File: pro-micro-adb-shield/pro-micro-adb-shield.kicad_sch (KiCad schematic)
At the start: 9 parts, among them J1 Mini-DIN-4, SW1 SW_Push_Dual, SW2 SW_DIP_x04, U1 Arduino_Pro_Micro

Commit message: Fix shorted RST/GND through button
why does this sort of thing always show up the day after you
send the gerbers in to be manufactured >:(
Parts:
- removed SW1: SW_Push_Dual, Button_Switch_THT:SW_TH_Tactile_Omron_B3F-10xx, symbol Switch:SW_Push_Dual
- added SW1: SW_Push_Dual_Other_PinLayout, Button_Switch_THT:SW_TH_Tactile_Omron_B3F-10xx, symbol cnorthway:SW_Push_Dual_Other_PinLayout
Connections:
- net GND: now also SW1.3, SW1.4
- net RST: now also SW1.1, SW1.2
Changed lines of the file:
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@@
     (pin "2")
   )
-  (symbol (lib_id "Switch:SW_Push_Dual") (at 237.49 81.28 0) (unit 1)
+  (symbol (lib_id "cnorthway:SW_Push_Dual_Other_PinLayout") (at 237.49 81.28 0) (unit 1)
     (in_bom yes) (on_board yes) (fields_autoplaced)
     (property "Reference" "SW1" (id 0) (at 237.49 74.3924 0))
-    (property "Value" "SW_Push_Dual" (id 1) (at 237.49 77.1675 0))
+    (property "Value" "SW_Push_Dual_Other_PinLayout" (id 1) (at 237.49 77.1675 0))
     (property "Footprint" "Button_Switch_THT:SW_TH_Tactile_Omron_B3F-10xx" (id 2) (at 237.49 76.2 0)
       (effects (font (size 1.27 1.27)) hide)
@@
       (reference "R3") (unit 1) (value "1k") (footprint "Resistor_THT:R_Axial_DIN0207_L6.3mm_D2.5mm_P10.16mm_Horizontal")
     )
-    (path "/053da573-106f-4526-842e-11ea387a9466"
-      (reference "SW1") (unit 1) (value "SW_Push_Dual") (footprint "Button_Switch_THT:SW_TH_Tactile_Omron_B3F-10xx")
+    (path "/9847d598-c40f-4c1c-9bbd-b8eb61f19e69"
+      (reference "SW1") (unit 1) (value "SW_Push_Dual_Other_PinLayout") (footprint "Button_Switch_THT:SW_TH_Tactile_Omron_B3F-10xx")
     )
     (path "/b88a04db-06e7-42bf-b775-d7f1fe8b90ce"

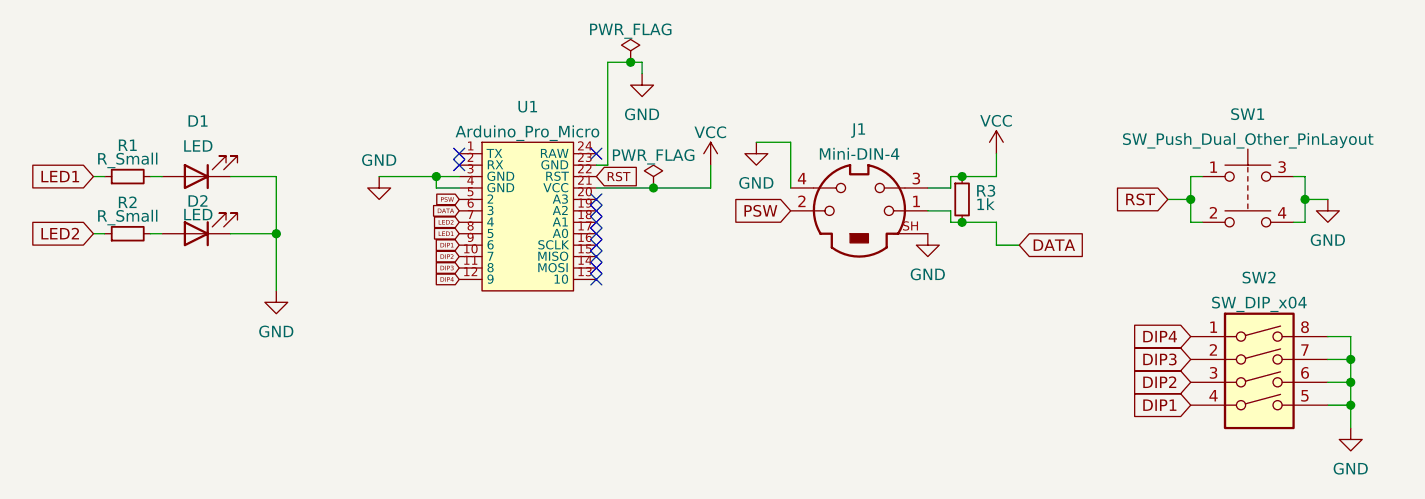
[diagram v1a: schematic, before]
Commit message: Use env var for 3d models, flip net names for DIP
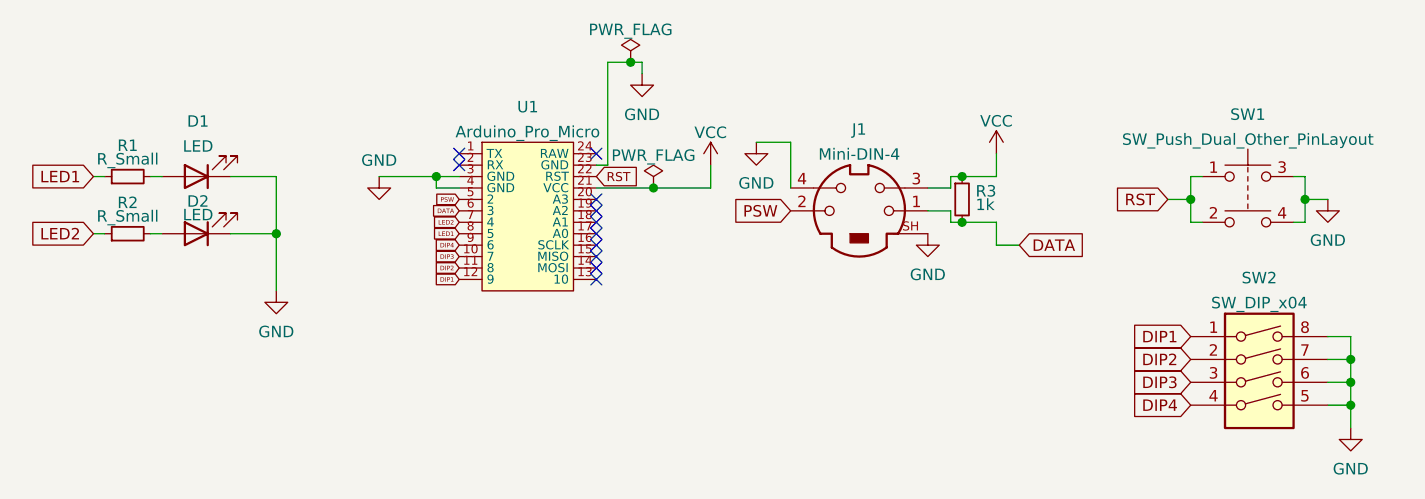
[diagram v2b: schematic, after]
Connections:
- net DIP1: now also SW2.1, U1.12 (9); no longer SW2.4, U1.9 (6)
- net DIP2: now also SW2.2, U1.11 (8); no longer SW2.3, U1.10 (7)
- net DIP3: now also SW2.3, U1.10 (7); no longer SW2.2, U1.11 (8)
- net DIP4: now also SW2.4, U1.9 (6); no longer SW2.1, U1.12 (9)
